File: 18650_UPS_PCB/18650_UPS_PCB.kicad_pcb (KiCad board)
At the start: 4 copper layers, 90 x 27.5 mm, 44 parts, among them J1 USB_B_Micro, J2 Conn_01x02, J3 Conn_01x02, SW1 SW_DIP_x02, U1 STLINK-V3MINI, U10 LR9102G-xx, U11 MP2667, U2 INA237, U3 EA_DOGS104N-A, U5 STM32L151RCTx

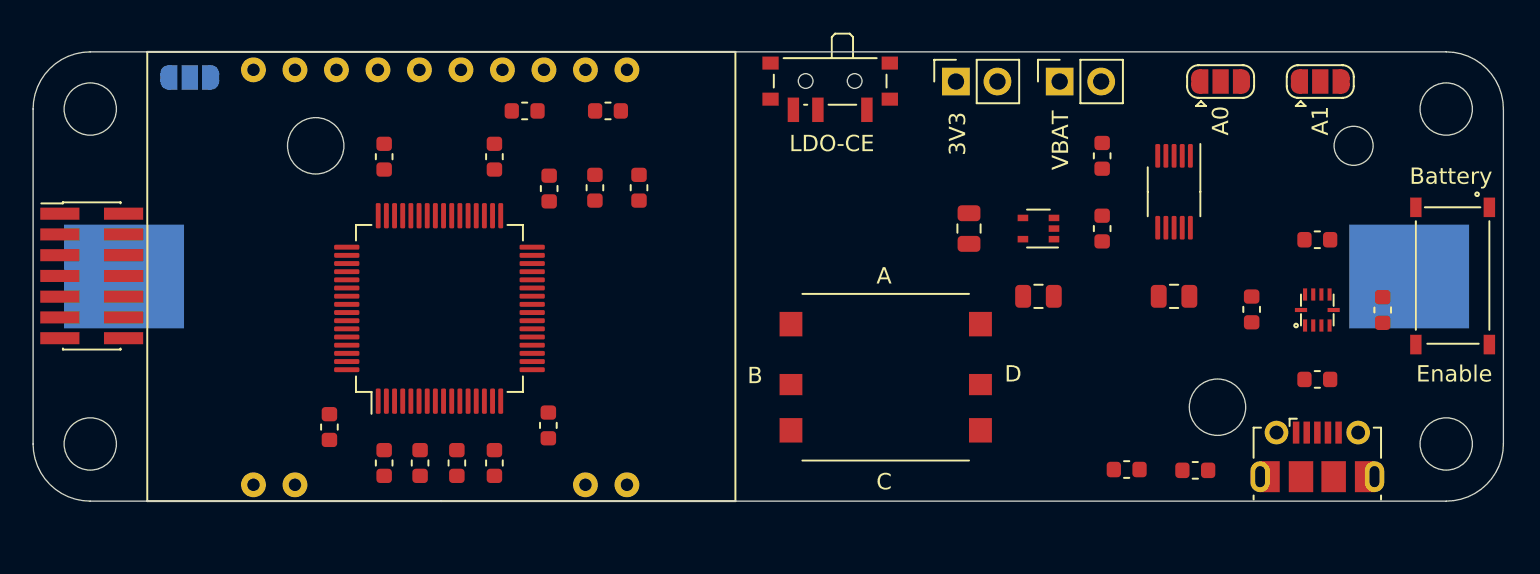
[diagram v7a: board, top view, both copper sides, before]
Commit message: Major Overhaul
Changed Buttons, Display changed to OLED and moved to top PCB
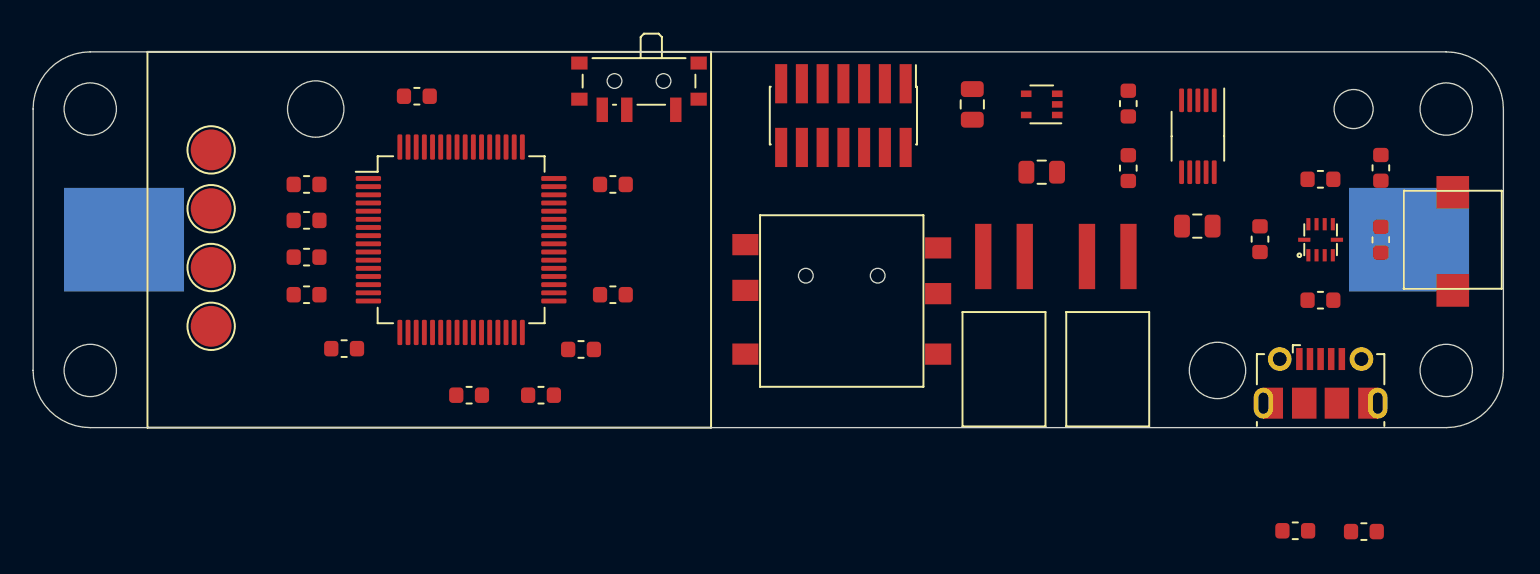
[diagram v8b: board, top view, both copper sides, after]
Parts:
- removed C2, C3: 1 uF, Capacitor_SMD:C_0603_1608Metric
- removed JP1: INA_ADR_0, Jumper:SolderJumper-3_P1.3mm_Open_RoundedPad1.0x1.5mm
- removed JP2: INA_ADR_1, Jumper:SolderJumper-3_P1.3mm_Open_RoundedPad1.0x1.5mm
- removed JP3: EA_ADR, Jumper:SolderJumper-3_P1.3mm_Open_RoundedPad1.0x1.5mm
- removed S1: TM-2027, CUSTOM_FOOTPRINTS:TM-2027
- added R6: 100 kOhm, Resistor_SMD:R_0603_1608Metric, F.Cu at (203.3, 81.3)
- added TP1: TestPoint, TestPoint:TestPoint_Pad_D2.5mm, F.Cu at (131.7, 80.2)
- added TP2: TestPoint, TestPoint:TestPoint_Pad_D2.5mm, F.Cu at (131.7, 83.8)
- added TP3: TestPoint, TestPoint:TestPoint_Pad_D2.5mm, F.Cu at (131.7, 87.4)
- added TP4: TestPoint, TestPoint:TestPoint_Pad_D2.5mm, F.Cu at (131.7, 91.0)
- J2, J3: footprint Connector_PinSocket_2.54mm:PinSocket_1x02_P2.54mm_Vertical -> CUSTOM_FOOTPRINTS:Pin_Socket_SMD_Horizontal_1x2
- SW1: value SW_DIP_x02 -> SW_SPST; footprint CUSTOM_FOOTPRINTS:TS6637TP-4P -> CUSTOM_FOOTPRINTS:ALPSALPINE_SKPMDAE011
- U3: value EA_DOGS104N-A -> BRIGHT_TSX103; footprint CUSTOM_FOOTPRINTS:EA_DOGS104N-A -> CUSTOM_FOOTPRINTS:BRIGHT_TSX103
- moved U1 47.0 mm to (170.4, 78.1), turned to 270 degrees
- moved U3 38.6 mm to (170.4, 87.0)
- moved C16 20.9 mm to (144.3, 76.9), turned to 0 degrees
- moved R2 17.7 mm to (137.6, 82.3), turned to 0 degrees
- moved R4 16.4 mm to (147.5, 95.2), turned to 0 degrees
- moved C5 16.4 mm to (137.6, 84.5), turned to 180 degrees
- moved C18 15.6 mm to (137.6, 86.8), turned to 180 degrees
- moved C17 15.4 mm to (137.6, 89.0), turned to 180 degrees
- moved R9 15.0 mm to (202.3, 103.5), turned to 0 degrees
- moved C14 14.1 mm to (156.3, 82.3), turned to 0 degrees
- moved C9 13.4 mm to (139.8, 92.3), turned to 180 degrees
- moved R5 13.1 mm to (151.9, 95.2), turned to 180 degrees
- moved LDO1 11.7 mm to (157.9, 76.3)
- moved C7 11.1 mm to (156.3, 89.0), turned to 0 degrees
- moved C12 10.0 mm to (154.3, 92.4), turned to 0 degrees
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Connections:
- SW1 pad 2: GND -> MP-INT
- U2 pad 1: Net-(JP2-Pad2) -> +3V3
- U2 pad 2: Net-(JP1-Pad2) -> +3V3
- U5 pad 41: EA-RST -> (no net)
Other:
- board size 90 x 27.5 mm -> 90 x 23 mm
- board text removed: "3V3"
- board text removed: "A"
- board text removed: "A0"
- board text removed: "A1"
- board text removed: "B"
- board text removed: "Battery"
- board text removed: "C"
- board text removed: "D"
- board text removed: "Enable"
- board text removed: "LDO-CE"
- board text removed: "VBAT"
